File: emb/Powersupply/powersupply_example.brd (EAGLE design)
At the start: 101.3 x 76.2 mm, 15 parts, among them IC1 7805TV, IC2 7812TV, IC3 LM2574N-5.0

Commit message: Updated PCB board
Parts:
- removed C1, C3: 22µF, rcl:E2,5-5
- moved SL1 44.0 mm to (2.54, 57.1), turned to 90 degrees
- moved C6 43.0 mm to (2.54, 52.1)
- moved IC1 42.3 mm to (11.4, 67.3), turned to 0 degrees
- moved C2 38.4 mm to (6.35, 73.7), turned to 180 degrees
- moved D1 34.2 mm to (11.4, 69.8), turned to 0 degrees
- moved L1 32.2 mm to (24.1, 38.1), turned to 90 degrees
- moved D3 30.9 mm to (15.2, 44.5), turned to 180 degrees
- moved C5 29.2 mm to (6.35, 33.0), turned to 180 degrees
- moved IC3 28.8 mm to (15.2, 38.1), turned to 180 degrees
- moved J1 27.6 mm to (10.2, 78.7), turned to 180 degrees
- moved IC2 19.7 mm to (12.7, 48.3), flipped to the bottom
- moved D2 17.8 mm to (12.7, 55.9), turned to 0 degrees
- moved C4 16.8 mm to (16.5, 59.7)
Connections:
- net 12V: now also J1.4; no longer J1.2
- net 15V: no longer C1.+, C3.+
- net 6V: now also J1.2; no longer J1.4
- net GND: no longer C1.-, C3.-
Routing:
- net GND: track 75.5 -> 0.00 mm
- net 5V: track 20.1 -> 79.4 mm
- net N$1: track 38.4 -> 0.00 mm
- net 15V: track 77.0 -> 53.6 mm
- net 6V: track 37.9 -> 20.5 mm
- net 12V: track 16.9 -> 30.6 mm
- net N$2: track 10.3 -> 0.00 mm
- net N$4: track 12.4 -> 19.1 mm
- added copper zone on layer 16, net GND
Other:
- board size 101.3 x 76.2 mm -> 101.3 x 81.3 mm

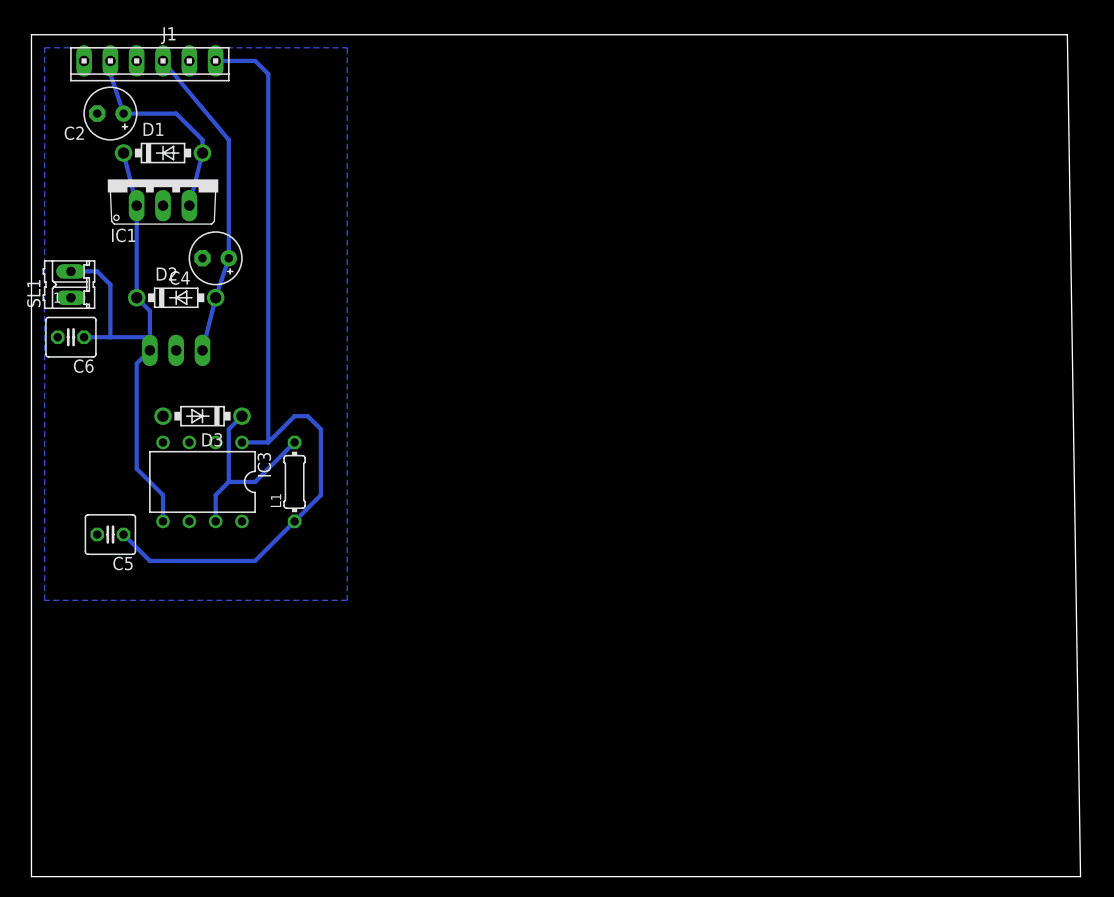
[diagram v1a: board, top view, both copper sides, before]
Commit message: Communication both directions + updated power supply board
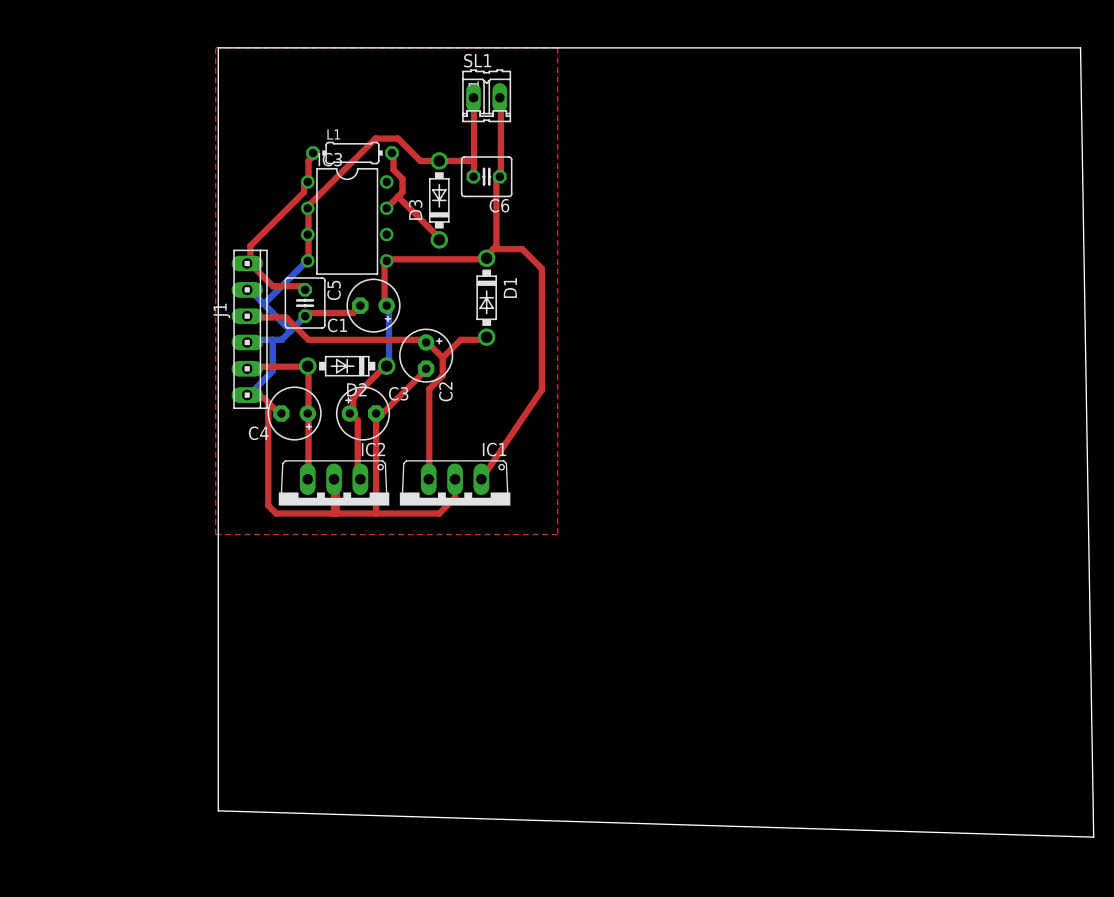
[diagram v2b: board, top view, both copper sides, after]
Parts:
- added C1, C3: 22µF, rcl:E2,5-5
- moved SL1 44.0 mm to (42.7, 75.2), turned to 0 degrees
- moved C6 43.0 mm to (42.7, 67.6)
- moved IC1 42.3 mm to (39.6, 35.8), turned to 180 degrees
- moved C2 38.4 mm to (36.8, 50.3), turned to 270 degrees
- moved D1 34.2 mm to (42.7, 55.9), turned to 270 degrees
- moved L1 32.2 mm to (29.7, 69.8), turned to 0 degrees
- moved D3 30.9 mm to (38.1, 65.3), turned to 90 degrees
- moved C5 29.2 mm to (25.1, 55.4), turned to 270 degrees
- moved IC3 28.8 mm to (29.2, 63.2), turned to 270 degrees
- moved J1 27.6 mm to (19.6, 52.8), turned to 270 degrees
- moved IC2 19.7 mm to (27.9, 35.8), flipped to the top
- moved D2 17.8 mm to (29.2, 49.3), turned to 180 degrees
- moved C4 16.8 mm to (24.1, 44.7)
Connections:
- net 12V: now also J1.2; no longer J1.4
- net 15V: now also C1.+, C3.+
- net 6V: now also J1.4; no longer J1.2
- net GND: now also C1.-, C3.-
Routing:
- net GND: track 0.00 -> 75.5 mm
- net 5V: track 79.4 -> 20.1 mm
- net N$1: track 0.00 -> 38.4 mm
- net 15V: track 53.6 -> 77.0 mm
- net 6V: track 20.5 -> 37.9 mm
- net 12V: track 30.6 -> 16.9 mm
- net N$2: track 0.00 -> 10.3 mm
- net N$4: track 19.1 -> 12.4 mm
- added copper zone on layer 1, net GND
- removed copper zone on layer 16, net GND
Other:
- board size 101.3 x 81.3 mm -> 84.5 x 76.2 mm

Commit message: wrong file
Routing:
- net N$1: track 38.4 -> 42.3 mm
- net N$3: track 0.00 -> 1.43 mm
- net N$2: track 10.3 -> 11.7 mm
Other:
- board text added: "Power supply"
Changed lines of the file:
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@@
 <?xml version="1.0" encoding="utf-8"?>
 <!DOCTYPE eagle SYSTEM "eagle.dtd">
-<eagle version="7.4.0">
+<eagle version="6.6.0">
 <drawing>
 <settings>
@@
 <setting verticaltext="up"/>
 </settings>
-<grid distance="0.05" unitdist="inch" unit="inch" style="lines" multiple="1" display="yes" altdistance="0.025" altunitdist="inch" altunit="inch"/>
+<grid distance="0.001" unitdist="inch" unit="inch" style="lines" multiple="1" display="yes" altdistance="0.025" altunitdist="inch" altunit="inch"/>
 <layers>
 <layer number="1" name="Top" color="4" fill="1" visible="yes" active="yes"/>
@@
 <wire x1="100" y1="80" x2="16.764" y2="80" width="0" layer="20"/>
 <wire x1="16.764" y1="80" x2="16.764" y2="6.35" width="0" layer="20"/>
+<text x="17.5514" y="77.216" size="1.778" layer="1">Power supply</text>
+<text x="32.2326" y="74.6506" size="1.778" layer="16" rot="MR0">Power supply</text>
 </plain>
 <attributes>
@@
 <pass name="Default">
 <param name="RoutingGrid" value="12.5mil"/>
-<param name="AutoGrid" value="1"/>
-<param name="Efforts" value="0"/>
-<param name="TopRouterVariant" value="1"/>
 <param name="tpViaShape" value="round"/>
 <param name="PrefDir.1" value="-"/>
@@
 <signal name="N$1">
 <wire x1="32.004" y1="44.45" x2="32.004" y2="35.052" width="0.6096" layer="1"/>
-<wire x1="32.004" y1="35.052" x2="27.94" y2="35.052" width="0.6096" layer="1"/>
+<wire x1="32.004" y1="35.052" x2="29.2608" y2="35.052" width="0.6096" layer="1"/>
+<wire x1="29.2608" y1="35.052" x2="27.94" y2="35.052" width="0.6096" layer="1"/>
 <wire x1="27.94" y1="35.052" x2="27.94" y2="39.116" width="0.6096" layer="1"/>
 <wire x1="27.94" y1="39.116" x2="28.194" y2="39.116" width="0.6096" layer="1"/>
 <wire x1="28.194" y1="39.116" x2="28.194" y2="35.052" width="0.6096" layer="1"/>
-<wire x1="28.194" y1="35.052" x2="22.352" y2="35.052" width="0.6096" layer="1"/>
+<wire x1="28.194" y1="35.052" x2="26.8732" y2="35.052" width="0.6096" layer="1"/>
+<wire x1="26.6446" y1="35.052" x2="22.352" y2="35.052" width="0.6096" layer="1"/>
 <wire x1="22.352" y1="35.052" x2="21.59" y2="35.814" width="0.6096" layer="1"/>
 <wire x1="21.59" y1="35.814" x2="21.59" y2="45.466" width="0.6096" layer="1"/>
+<wire x1="28.0162" y1="36.2966" x2="29.0576" y2="35.2552" width="0.6096" layer="1"/>
+<wire x1="29.2608" y1="35.052" x2="29.0576" y2="35.2552" width="0.6096" layer="1"/>
+<wire x1="29.0576" y1="35.2552" x2="28.5242" y2="35.2552" width="0.6096" layer="1"/>
+<wire x1="28.0162" y1="36.195" x2="26.8732" y2="35.052" width="0.6096" layer="1"/>
+<wire x1="26.8732" y1="35.052" x2="26.6446" y2="35.052" width="0.6096" layer="1"/>
 </signal>
 <signal name="N$2">
 <wire x1="39.624" y1="38.862" x2="39.624" y2="36.576" width="0.6096" layer="1"/>
 <wire x1="39.624" y1="36.576" x2="38.1" y2="35.052" width="0.6096" layer="1"/>
-<wire x1="38.1" y1="35.052" x2="32.258" y2="35.052" width="0.6096" layer="1"/>
+<wire x1="38.1" y1="35.052" x2="33.2486" y2="35.052" width="0.6096" layer="1"/>
+<wire x1="32.9438" y1="35.052" x2="32.258" y2="35.052" width="0.6096" layer="1"/>
+<wire x1="31.9532" y1="36.0426" x2="32.9438" y2="35.052" width="0.6096" layer="1"/>
+<wire x1="32.9438" y1="35.052" x2="33.2486" y2="35.052" width="0.6096" layer="1"/>
+</signal>
+<signal name="N$3">
+<wire x1="31.9278" y1="36.0426" x2="30.988" y2="35.1028" width="0.6096" layer="1"/>
+<wire x1="30.988" y1="35.1028" x2="30.8864" y2="35.1028" width="0.6096" layer="1"/>
 </signal>
 </signals>
